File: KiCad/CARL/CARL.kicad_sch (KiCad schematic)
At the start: 39 parts, among them J1 Barrel_Jack (5V DC Supply), J2 SD_Card_Device, U1 NHD-0420H1Z (LCD), U2 LM386, U3 Led Driver

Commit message: Update CARL.kicad_sch
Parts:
- removed J2: SD_Card_Device, symbol Connector:SD_Card_Device
- removed U2: LM386, symbol Amplifier_Audio:LM386
- removed U3: Led Driver, Package_DFN_QFN:QFN-24-1EP_4x4mm_P0.5mm_EP2.15x2.15mm, symbol Driver_LED:LED1642GWQTR
- added R17, R18, R19, R20, R21, R22, R23, R24, R25, R26: R_Small_US, symbol Device:R_Small_US
- added RV2: R_Potentiometer_US, symbol Device:R_Potentiometer_US
- added SW1, SW2, SW3, SW4, SW5, SW6, SW7, SW8, SW9: SW_Push, symbol Switch:SW_Push
- added SW10: Power Switch, symbol Switch:SW_SPST
- added U2: MIC5365-3.3YC5 (5V to 3.3V regulator), Package_TO_SOT_SMD:SOT-353_SC-70-5, symbol Regulator_Linear:MIC5365-3.3YC5
- added U3: MAX98357A (Amplifier), Package_DFN_QFN:TQFN-16-1EP_3x3mm_P0.5mm_EP1.23x1.23mm, symbol Audio:MAX98357A
- added U4: TLC5947DAP (LED Driver), Package_SO:HTSSOP-32-1EP_6.1x11mm_P0.65mm_EP5.2x11mm_Mask4.11x4.36mm_ThermalVias, symbol Driver_LED:TLC5947DAP
- LS1: value Speaker -> Speaker 8Ohm, 3" Diameter
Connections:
- net 3.3V: now also A1.10 (IO4/A5), A1.11 (SCK/IO5), A1.16 (IO21), A1.19 (A6/IO14), A1.20 (A7/IO32), A1.21 (A8/IO15), A1.5 (DAC2/A0), A1.6 (DAC1/A1), A1.9 (IO36/A4), SW1.2, SW2.2, SW3.2, SW4.2, SW5.2, SW6.2, SW7.2, SW8.2, SW9.2, U2.5 (VOUT)
- net 5V: now also RV2.1, SW10.2 (B), U2.1 (VIN), U2.3 (EN), U3.7 (VDD), U3.8 (VDD), U4.32 (VCC); no longer J1.1
- net GND: now also R17.1, R18.1, R19.1, R20.1, R21.1, R22.1, R23.1, R24.1, R25.1, R26.1, RV2.3, U2.2 (GND), U3.11 (GND), U3.15 (GND), U3.3 (GND), U4.1 (GND); no longer LS1.2
- net at D13.2 (A): now also U4.17 (OUT12)
- net at A1.14 (RX/IO16): now also U4.29 (SOUT)
- net at A1.15 (TX/IO17): now also U4.4 (SIN)
- net at A1.17 (SDA/IO23): now also U3.14 (LRCLK)
- net at A1.18 (SCL/IO22): now also U3.16 (BCLK), U4.3 (SCLK)
- net at A1.7 (I34/A2): now also U3.1 (DIN)
- net at A1.8 (I39/A3): now also U3.4 (~{SD_MODE})
- net at LS1.1: now also U3.9 (OUTP); no longer A1.9 (IO36/A4)
- net at D4.2 (A): now also U4.8 (OUT3)
- net at D14.2 (A): now also U4.18 (OUT13)
- net at D9.2 (A): now also U4.13 (OUT8)
- net at D10.2 (A): now also U4.14 (OUT9)
- net at D11.2 (A): now also U4.15 (OUT10)
- net at D12.2 (A): now also U4.16 (OUT11)
- net at D15.2 (A): now also U4.19 (OUT14)
- net at D16.2 (A): now also U4.20 (OUT15)
- net at D1.2 (A): now also U4.5 (OUT0)
- net at D2.2 (A): now also U4.6 (OUT1)
- net at D3.2 (A): now also U4.7 (OUT2)
- net at D5.2 (A): now also U4.9 (OUT4)
- net at D6.2 (A): now also U4.10 (OUT5)
- net at D7.2 (A): now also U4.11 (OUT6)
- net at D8.2 (A): now also U4.12 (OUT7)
- new net: R26.2, SW9.1
- new net: LS1.2, U3.10 (OUTN)
- new net: RV2.2, U3.2 (GAIN_SLOT)
- new net: R25.2, SW8.1
- new net: R21.2, SW4.1
- new net: R20.2, SW3.1
- new net: R23.2, SW6.1
- new net: J1.1, SW10.1 (A)
- new net: R18.2, SW1.1
- new net: R22.2, SW5.1
- new net: R19.2, SW2.1
- new net: R24.2, SW7.1
- new net: R17.2, U4.31 (IREF)
- no-connect marks 4 -> 13
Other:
- note added: "Beat Display LEDs"
- note added: "Beat Input Buttoms"
- note added: "Channel Select/Start Playback Button"
- moved on the sheet: J1, LS1

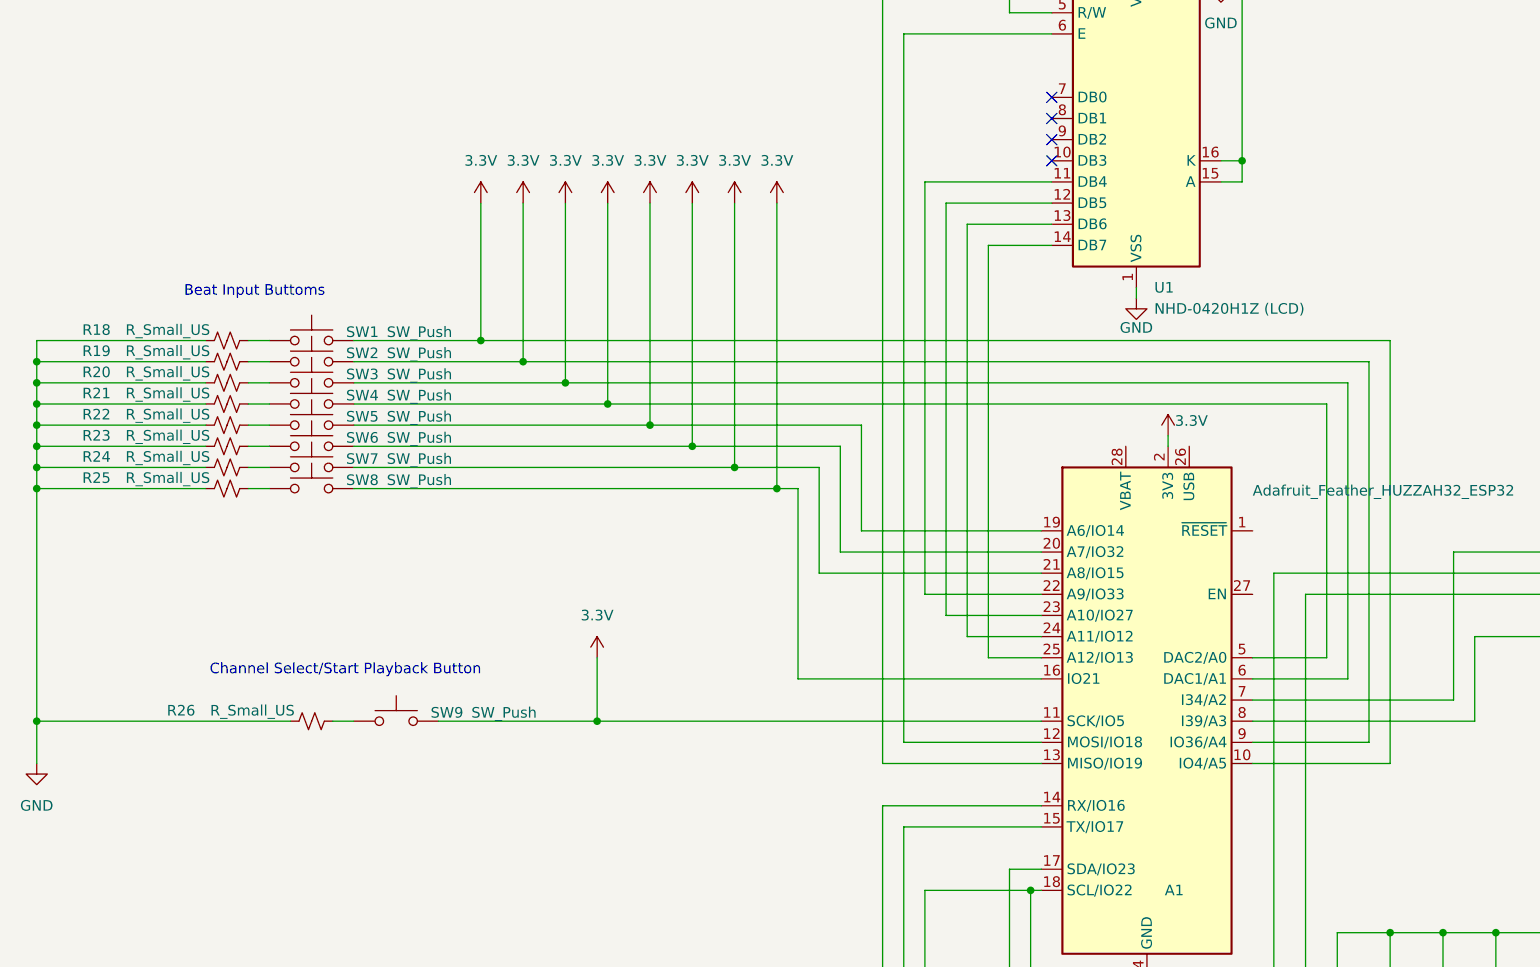
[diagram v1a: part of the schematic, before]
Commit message: Update CARL.kicad_sch
Edited button layout to work correctly and removed resistors so we can instead utilize the ESP32's built in pullup resistor functionality.
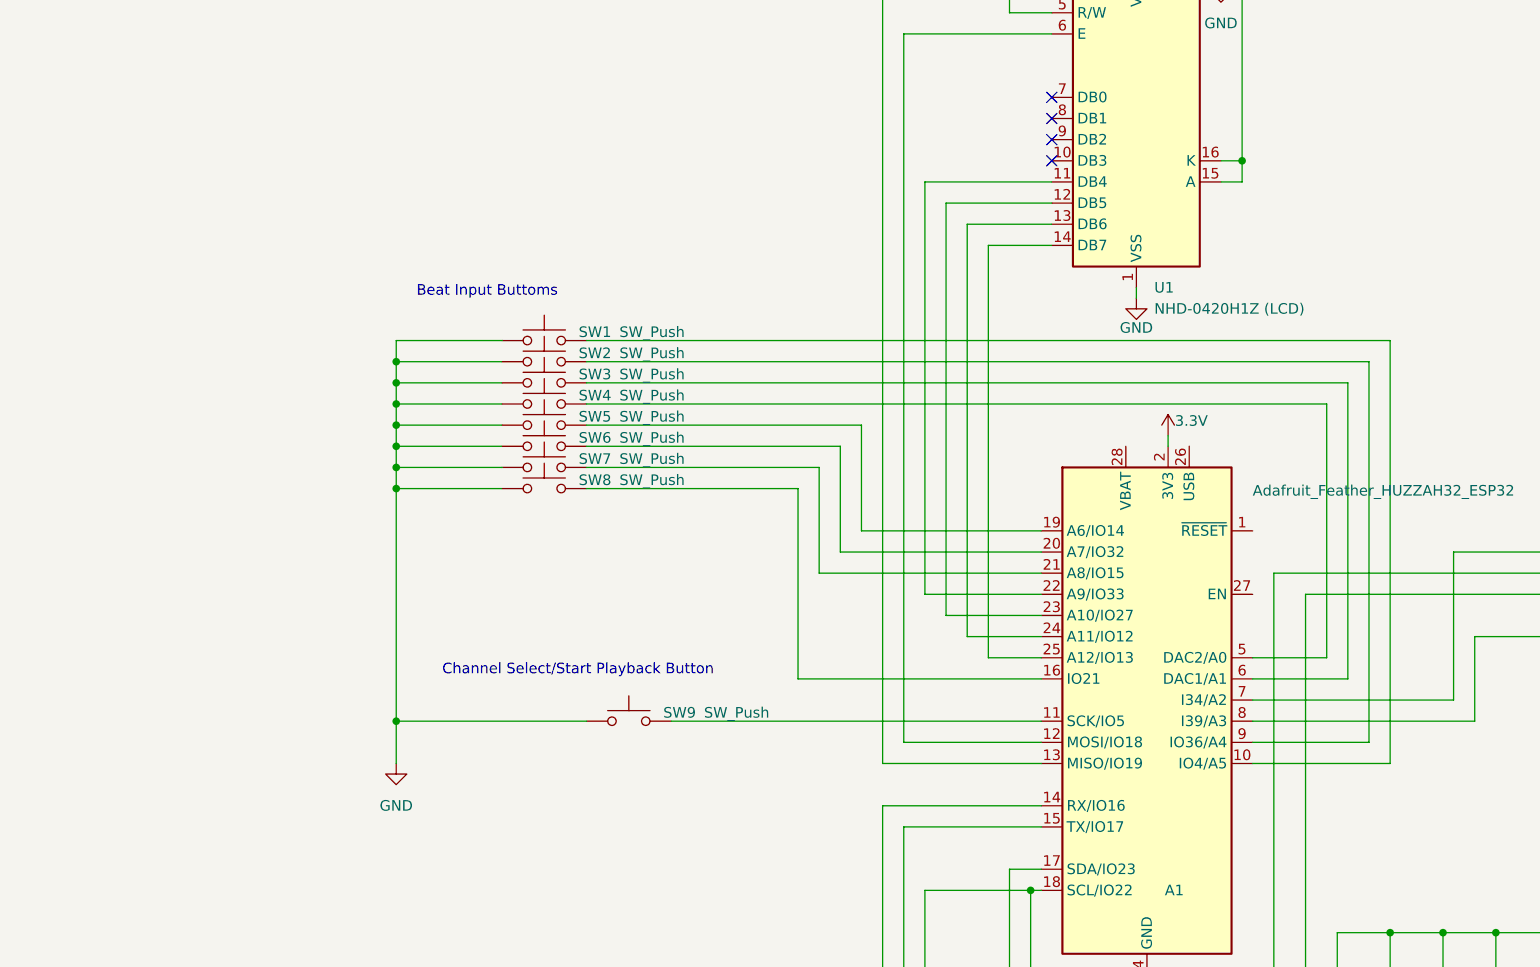
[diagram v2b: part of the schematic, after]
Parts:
- removed R18, R19, R20, R21, R22, R23, R24, R25, R26: R_Small_US, symbol Device:R_Small_US
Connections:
- net 3.3V: no longer A1.10 (IO4/A5), A1.11 (SCK/IO5), A1.16 (IO21), A1.19 (A6/IO14), A1.20 (A7/IO32), A1.21 (A8/IO15), A1.5 (DAC2/A0), A1.6 (DAC1/A1), A1.9 (IO36/A4), SW1.2, SW2.2, SW3.2, SW4.2, SW5.2, SW6.2, SW7.2, SW8.2, SW9.2
- net GND: now also SW1.1, SW2.1, SW3.1, SW4.1, SW5.1, SW6.1, SW7.1, SW8.1, SW9.1
- new net: A1.16 (IO21), SW8.2
- new net: A1.10 (IO4/A5), SW1.2
- new net: A1.11 (SCK/IO5), SW9.2
- new net: A1.19 (A6/IO14), SW5.2
- new net: A1.20 (A7/IO32), SW6.2
- new net: A1.21 (A8/IO15), SW7.2
- new net: A1.5 (DAC2/A0), SW4.2
- new net: A1.6 (DAC1/A1), SW3.2
- new net: A1.9 (IO36/A4), SW2.2
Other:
- moved on the sheet: SW1, SW2, SW3, SW4, SW5, SW6, SW7, SW8, SW9

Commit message: Preliminary Schematic Revision 2
Fixed connections to LCD. Edited connections to Amplifier to (hopefully) work. Added GPIO extender and moved all button connections off of the esp32 and onto the extender.
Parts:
- added SW11: Mute_Button, symbol Switch:SW_Push
- added SW12: Move_Left_Button, symbol Switch:SW_Push
- added SW13: Move_Right_Button, symbol Switch:SW_Push
- added SW14: Play_Button, symbol Switch:SW_Push
- added U5: MCP23017_SO, Package_SO:SOIC-28W_7.5x17.9mm_P1.27mm, symbol Interface_Expansion:MCP23017_SO
- SW9: value SW_Push -> Save_and_Load_Button
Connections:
- net 3.3V: now also U1.15 (A), U5.17 (A2), U5.9 (VDD)
- net GND: now also SW11.1, SW12.1, SW13.1, SW14.1, U5.10 (VSS), U5.15 (A0), U5.16 (A1); no longer U1.15 (A)
- net at U3.14 (LRCLK): now also A1.9 (IO36/A4); no longer A1.17 (SDA/IO23)
- net at A1.18 (SCL/IO22), U4.3 (SCLK): now also U5.12 (SCK); no longer U3.16 (BCLK)
- net at A1.8 (I39/A3): now also U3.16 (BCLK); no longer U3.4 (~{SD_MODE})
- net at SW8.2: now also U5.8 (GPB7); no longer A1.16 (IO21)
- net at A1.10 (IO4/A5): now also U3.4 (~{SD_MODE}); no longer SW1.2
- net at A1.11 (SCK/IO5): now also U1.4 (RS); no longer SW9.2
- net at A1.13 (MISO/IO19): no longer U1.4 (RS)
- net at A1.19 (A6/IO14): now also U5.19 (INTB); no longer SW5.2
- net at A1.20 (A7/IO32): now also U5.20 (INTA); no longer SW6.2
- net at A1.21 (A8/IO15): no longer SW7.2
- net at A1.5 (DAC2/A0): no longer SW4.2
- net at A1.6 (DAC1/A1): no longer SW3.2
- net at SW2.2: now also U5.2 (GPB1); no longer A1.9 (IO36/A4)
- new net: SW13.2, U5.24 (GPA3)
- new net: A1.17 (SDA/IO23), U5.13 (SDA)
- new net: SW1.2, U5.1 (GPB0)
- new net: SW9.2, U5.21 (GPA0)
- new net: SW11.2, U5.22 (GPA1)
- new net: SW12.2, U5.23 (GPA2)
- new net: SW14.2, U5.25 (GPA4)
- new net: SW3.2, U5.3 (GPB2)
- new net: SW4.2, U5.4 (GPB3)
- new net: SW5.2, U5.5 (GPB4)
- new net: SW6.2, U5.6 (GPB5)
- new net: SW7.2, U5.7 (GPB6)
- no-connect marks 13 -> 29
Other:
- note added: "Says SCK (SPI clock) but chip uses I2C (SLC). Odd pin labeling or error on our part?"
- note removed: "Channel Select/Start Playback Button"
- title: (none) -> CARL
- moved on the sheet: SW1, SW2, SW3, SW4, SW5, SW6, SW7, SW8, SW9

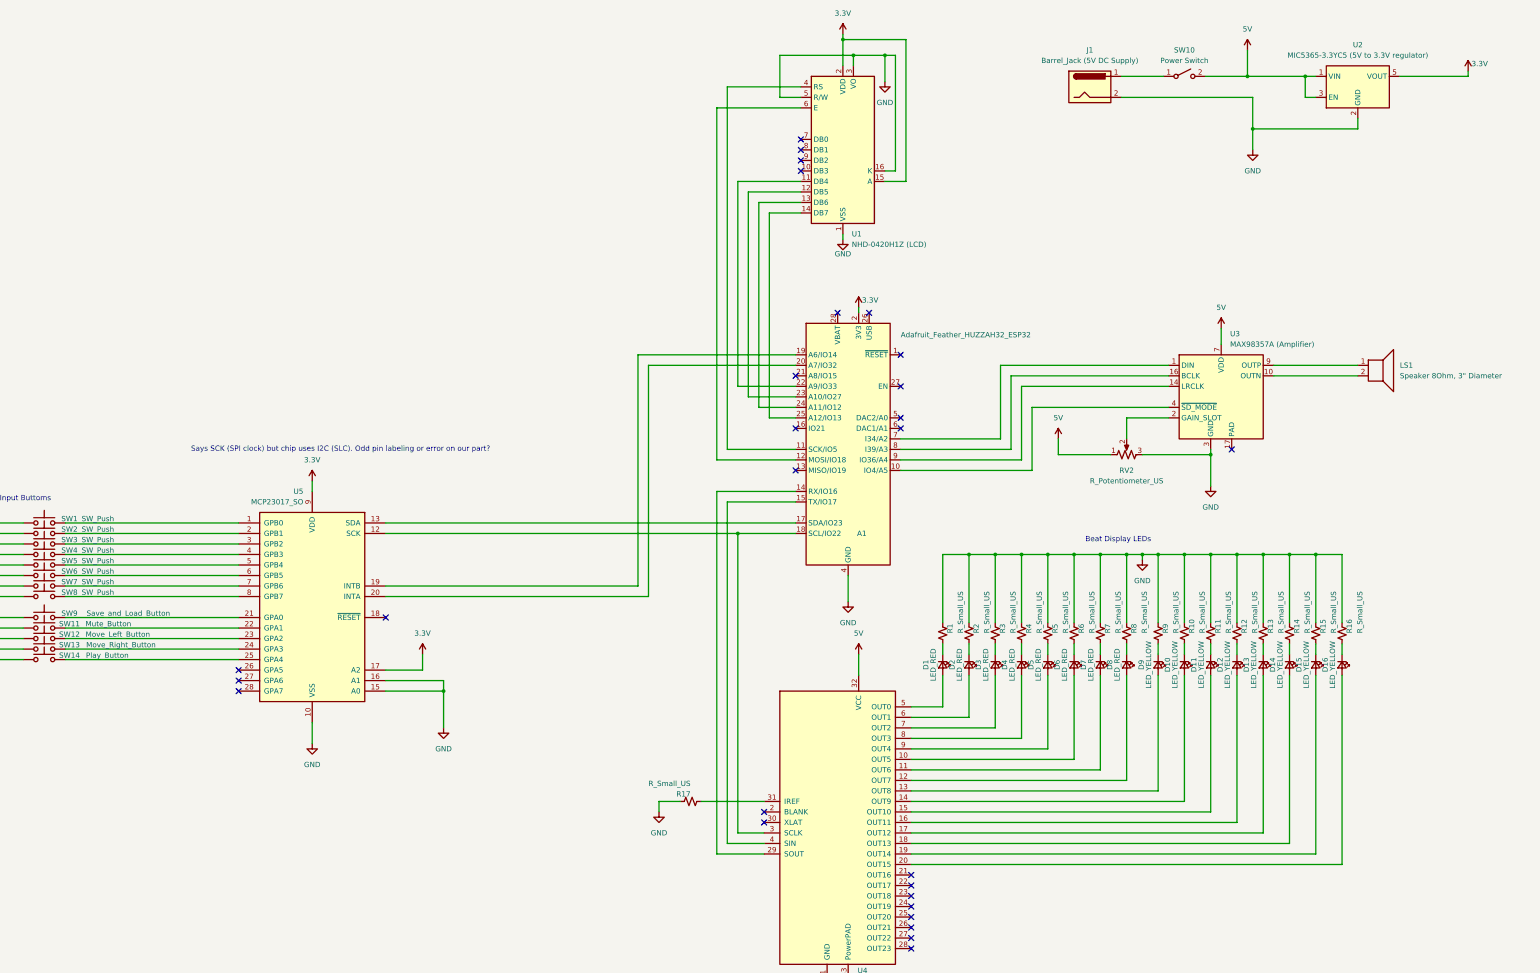
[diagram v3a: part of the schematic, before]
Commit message: Schematic Update / Preliminary PCB
-Added remaining LEDs to the schematic
-Edited some connections with the amplifier to function correctly (hopefully)
-Edited connections between LEDs and LED driver to correspond with what the data sheet shows. The LEDs now receive VCC instead of GND and all resistors have been removed from them with a new one added on the IREF pin.
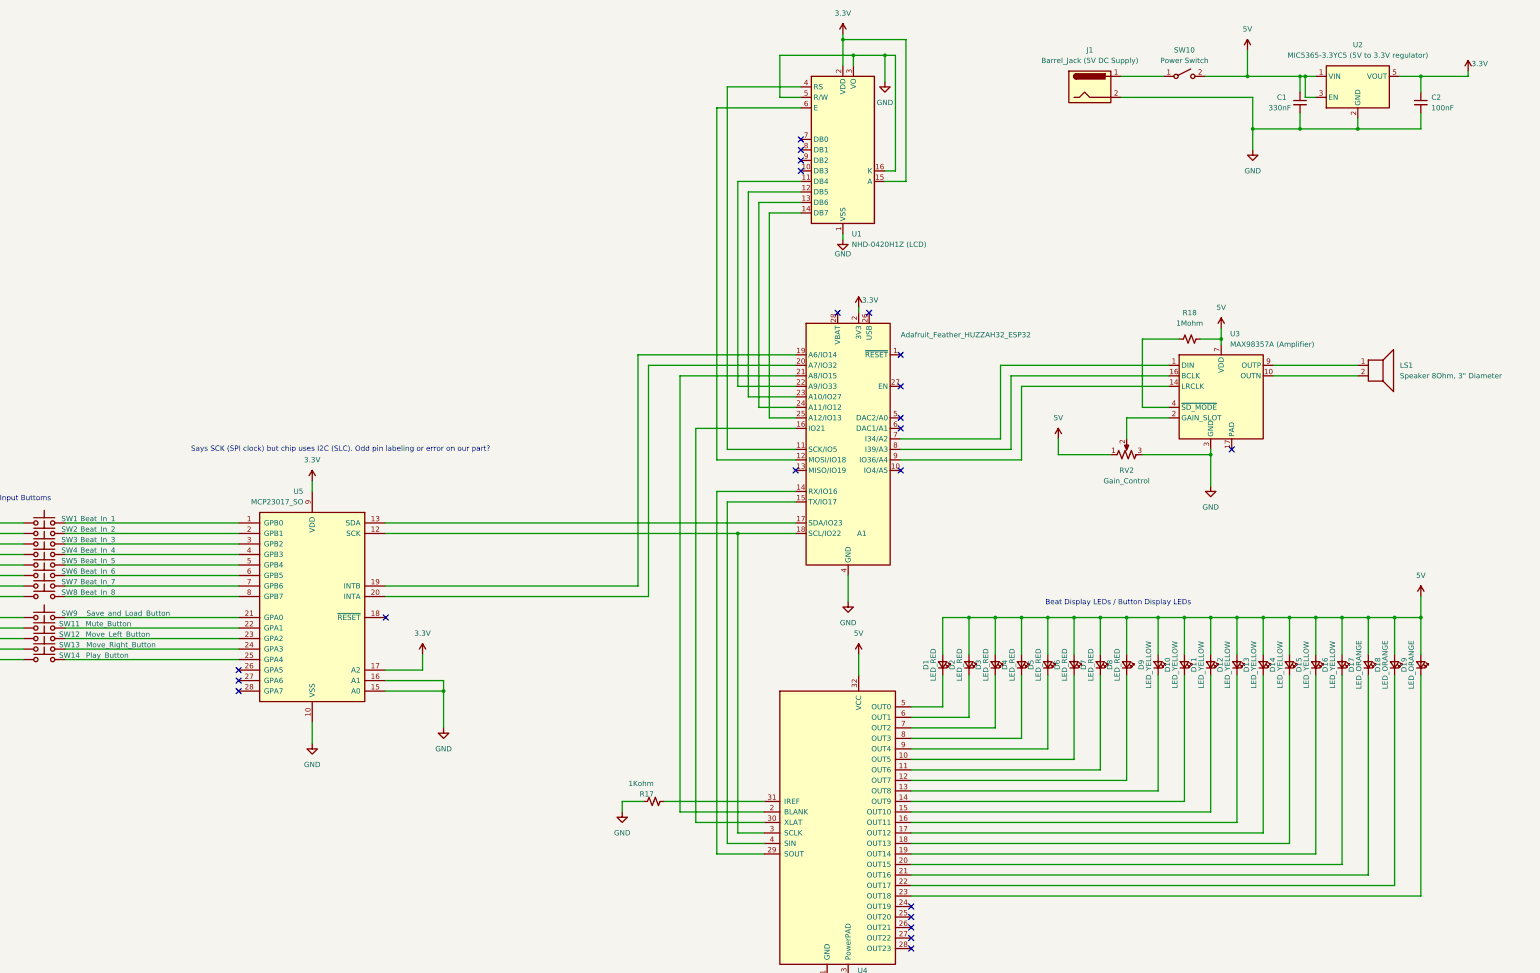
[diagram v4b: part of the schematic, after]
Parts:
- removed R1, R10, R11, R12, R13, R14, R15, R16, R2, R3, R4, R5, R6, R7, R8, R9: R_Small_US, symbol Device:R_Small_US
- added C1: 330nF, Capacitor_SMD:C_0805_2012Metric, symbol Device:C_Small
- added C2: 100nF, Capacitor_SMD:C_0805_2012Metric, symbol Device:C_Small
- added D17, D18, D19: LED_ORANGE, LED_SMD:LED_0805_2012Metric, symbol Device:LED_Small
- added R18: 1Mohm, Resistor_SMD:R_0805_2012Metric, symbol Device:R_Small_US
- D1, D10, D11, D12, D13, D14, D15, D16, D2, D3, D4, D5, D6, D7, D8, D9: footprint (none) -> LED_SMD:LED_0805_2012Metric
- J1: footprint (none) -> Connector_BarrelJack:BarrelJack_CUI_PJ-036AH-SMT_Horizontal
- LS1: footprint (none) -> Buzzer_Beeper:Speaker_CUI_CMR-1206S-67
- R17: value R_Small_US -> 1Kohm; footprint (none) -> Resistor_SMD:R_0805_2012Metric
- RV2: value R_Potentiometer_US -> Gain_Control; footprint (none) -> Potentiometer_THT:Potentiometer_Bourns_3009Y_Horizontal
- SW1: value SW_Push -> Beat_In_1; footprint (none) -> Button_Switch_Keyboard:SW_Cherry_MX_1.00u_PCB
- SW10, SW11, SW12, SW13, SW14, SW9: footprint (none) -> Button_Switch_Keyboard:SW_Cherry_MX_1.00u_PCB
- SW2: value SW_Push -> Beat_In_2; footprint (none) -> Button_Switch_Keyboard:SW_Cherry_MX_1.00u_PCB
- SW3: value SW_Push -> Beat_In_3; footprint (none) -> Button_Switch_Keyboard:SW_Cherry_MX_1.00u_PCB
- SW4: value SW_Push -> Beat_In_4; footprint (none) -> Button_Switch_Keyboard:SW_Cherry_MX_1.00u_PCB
- SW5: value SW_Push -> Beat_In_5; footprint (none) -> Button_Switch_Keyboard:SW_Cherry_MX_1.00u_PCB
- SW6: value SW_Push -> Beat_In_6; footprint (none) -> Button_Switch_Keyboard:SW_Cherry_MX_1.00u_PCB
- SW7: value SW_Push -> Beat_In_7; footprint (none) -> Button_Switch_Keyboard:SW_Cherry_MX_1.00u_PCB
- SW8: value SW_Push -> Beat_In_8; footprint (none) -> Button_Switch_Keyboard:SW_Cherry_MX_1.00u_PCB
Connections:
- net 3.3V: now also C2.1
- net 5V: now also D1.2 (A), D10.2 (A), D11.2 (A), D12.2 (A), D13.2 (A), D14.2 (A), D15.2 (A), D16.2 (A), D2.2 (A), D3.2 (A), D4.2 (A), D5.2 (A), D6.2 (A), D7.2 (A), D8.2 (A), D9.2 (A), C1.1, D17.2 (A), D18.2 (A), D19.2 (A), R18.2
- net GND: now also C1.2, C2.2
- net at D13.1 (K): now also U4.17 (OUT12)
- net at D4.1 (K): now also U4.8 (OUT3)
- net at U3.4 (~{SD_MODE}): now also R18.1; no longer A1.10 (IO4/A5)
- net at D10.1 (K): now also U4.14 (OUT9)
- net at A1.16 (IO21): now also U4.30 (XLAT)
- net at A1.21 (A8/IO15): now also U4.2 (BLANK)
- net at D3.1 (K): now also U4.7 (OUT2)
- net at D9.1 (K): now also U4.13 (OUT8)
- net at D14.1 (K): now also U4.18 (OUT13)
- net at D11.1 (K): now also U4.15 (OUT10)
- net at D8.1 (K): now also U4.12 (OUT7)
- net at D6.1 (K): now also U4.10 (OUT5)
- net at D15.1 (K): now also U4.19 (OUT14)
- net at D12.1 (K): now also U4.16 (OUT11)
- net at D5.1 (K): now also U4.9 (OUT4)
- net at D1.1 (K): now also U4.5 (OUT0)
- net at D2.1 (K): now also U4.6 (OUT1)
- net at D7.1 (K): now also U4.11 (OUT6)
- net at D16.1 (K): now also U4.20 (OUT15)
- net at U4.21 (OUT16): now also D17.1 (K)
- net at U4.22 (OUT17): now also D18.1 (K)
- net at U4.23 (OUT18): now also D19.1 (K)
- no-connect marks 29 -> 23
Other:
- note added: "Beat Display LEDs / Button Display LEDs"
- note removed: "Beat Display LEDs"
- moved on the sheet: R17
